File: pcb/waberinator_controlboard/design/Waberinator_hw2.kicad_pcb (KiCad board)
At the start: 4 copper layers, 49.5 x 99.5 mm, 119 parts, among them J1 Conn_01x04_Pin, J27 Conn_01x04, J28 Conn_01x04, J29 Conn_01x04, J4 Conn_01x06, J7 Conn_01x10_Pin, Q1 AOSP21321, Q10 Q_NPN_BEC, Q2 SISHA04DN-T1-GE3, Q3 SISHA04DN-T1-GE3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

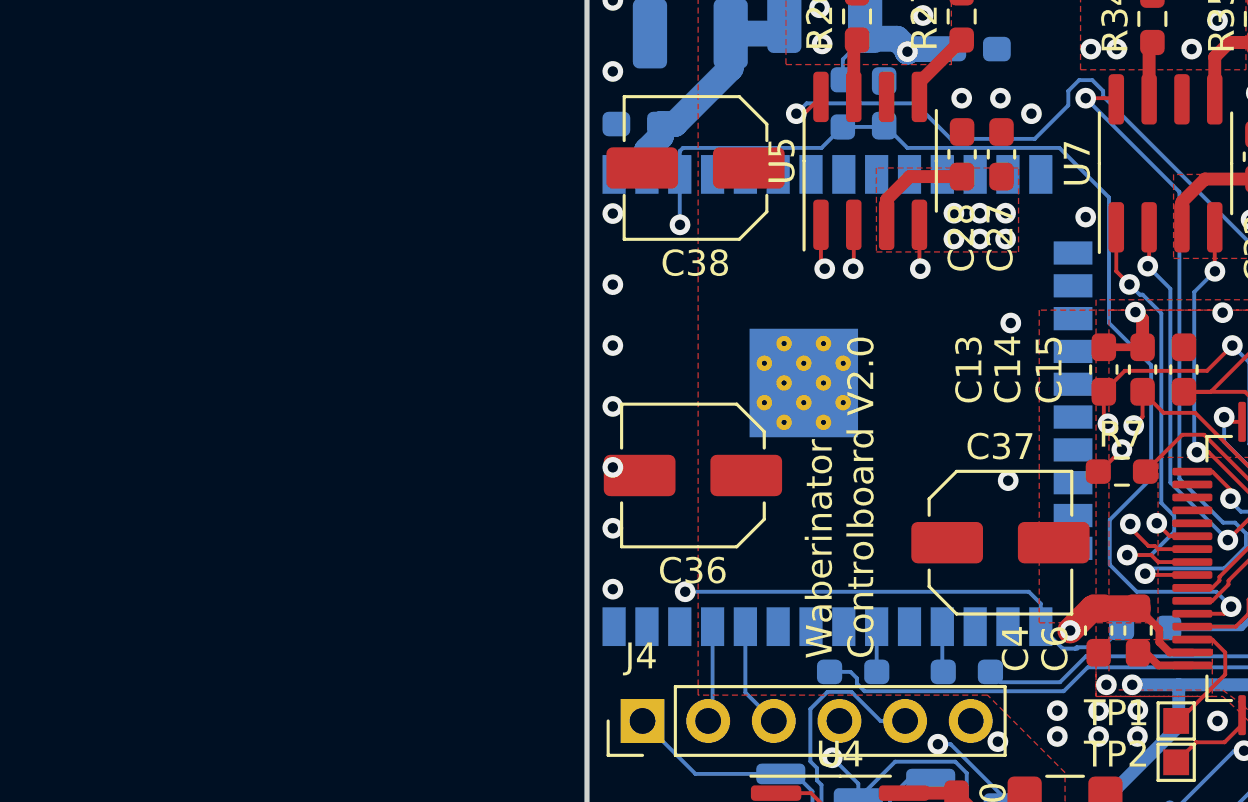
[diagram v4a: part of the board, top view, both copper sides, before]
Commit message: [HW] fix esp32 footprint and symbol
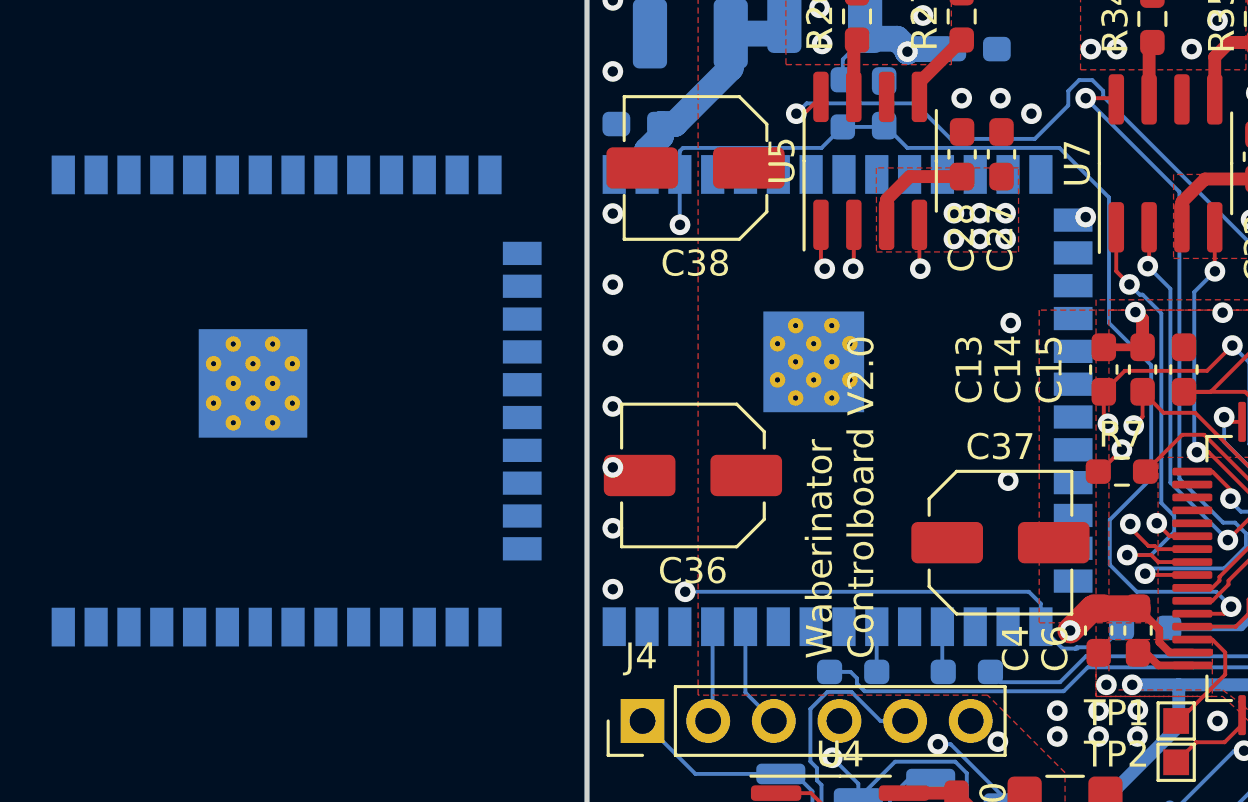
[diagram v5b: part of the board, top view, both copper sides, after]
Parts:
- added U9: ESP32-S3-WROOM-1, RF_Module:ESP32-S3-WROOM-1, B.Cu at (72.8, 166.1)
- moved U8 21.3 mm to (54.5, 166.1)
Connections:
- U8 pad 1: RET -> Net-(U8-GND-Pad1)
- U8 pad 15: RET -> Net-(U8-GND-Pad1)
- U8 pad 2: /esp32_vdd -> unconnected-(U8-VDD-Pad2)
- U8 pad 25: /esp32_io0 -> unconnected-(U8-IO0-Pad25)
- U8 pad 28: /U1TXD_ESP32 -> unconnected-(U8-IO17-Pad28)
- U8 pad 3: /esp32_en -> unconnected-(U8-EN-Pad3)
- U8 pad 30: /U1RXD_ESP32 -> unconnected-(U8-IO18-Pad30)
- U8 pad 34: /U0RXD_ESP32 -> unconnected-(U8-RXD0/IO3-Pad34)
- U8 pad 35: /U0TXD_ESP32 -> unconnected-(U8-TXD0/IO1-Pad35)
- U8 pad 38: RET -> Net-(U8-GND-Pad1)
- U8 pad 39: RET -> Net-(U8-GND-Pad1)
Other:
- board text added: "connect"
- board text added: "cut"

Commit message: [HW] misc changes
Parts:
- removed U8: ESP32-WROOM-32, RF_Module:ESP32-WROOM-32

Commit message: [HW] bugfixes
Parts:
- added U8: ESP32-WROOM-32, RF_Module:ESP32-WROOM-32, F.Cu at (31.9, 126.7)
- C39: value 1nF -> 1µF
- L1: value SRU1048-4R7Y -> 744325330
- R14, R18: value 12k -> 10k
- R15, R16: value R -> 120
- R17: value R -> 100
- R28: value 5k -> 10k
- RT1: value 117k -> 95k3
